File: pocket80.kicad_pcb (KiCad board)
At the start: 2 copper layers, 118 parts, among them J1 USB_C_Receptacle_USB2.0_14P, Q1 IRLML6402, Q2 BC847, SW1 F1, SW10 4, SW11 9, SW12 5, SW13 A, SW14 6, SW15 B, SW16 7, SW17 0, SW18 INC, SW19 1, SW2 F2, SW20 DEC, SW21 2, SW22 SEL, SW23 3, SW24 GO!, SW25 SW_Push_DPDT, SW3 F3, SW4 F4, SW5 C, SW6 D, SW7 E, SW8 F, SW9 8, U1 Z80CPU, U10 74HC00, U11 74HC138, U12 CH340N, U13 TP4056-42-ESOP8, U14 SX1308, U15 LM393, U2 74HC244, U3 PIO-PLCC-44, U4 SIO3-PLCC-44, U5 CTC-PLCC-44, U6 NE555D, U7 74HC04, U8 62256, U9 KM28C64A, Y1 3.6864M

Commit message: HW: Finish CTC sound generator
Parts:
- added C29: 1u, Capacitor_SMD:C_0805_2012Metric, B.Cu at (-73.7, 53.1)
- added C30: 100n, Capacitor_SMD:C_0805_2012Metric, F.Cu at (139.9, 88.2)
- added H1: MountingHole_Pad_MP, MountingHole:MountingHole_3.2mm_M3_Pad_Via, F.Cu at (40.6, 52.5)
- added H2: MountingHole_Pad_MP, MountingHole:MountingHole_3.2mm_M3_Pad_Via, F.Cu at (40.6, 60.4)
- added H3: MountingHole_Pad_MP, MountingHole:MountingHole_3.2mm_M3_Pad_Via, F.Cu at (40.6, 68.4)
- added H4: MountingHole_Pad_MP, MountingHole:MountingHole_3.2mm_M3_Pad_Via, F.Cu at (40.6, 76.3)
- added R32: 100k, Resistor_SMD:R_0805_2012Metric, B.Cu at (-73.9, 68.1)
- added U16: 74HC74, Package_SO:SO-14_3.9x8.65mm_P1.27mm, B.Cu at (-60.4, 48.2)
- LS1, Q2, R24, R25: moved to B.Cu
- moved Q2 254.7 mm to (-71.3, 50.2), turned to 180 degrees
- moved R24 249.8 mm to (-68.2, 50.2), turned to 90 degrees
- moved R25 248.5 mm to (-66.2, 50.2), turned to 90 degrees
- moved LS1 240.0 mm to (-68.6, 60.7)
- moved C19 86.0 mm to (229.6, 119.6), turned to 90 degrees
- moved C20 82.6 mm to (227.6, 119.6), turned to 90 degrees
- moved R13 76.8 mm to (222.2, 119.1), turned to 90 degrees
- moved R14 71.6 mm to (222.2, 115.6), turned to 90 degrees
- moved L1 68.5 mm to (226.8, 111.0), turned to 180 degrees
- moved R15 66.6 mm to (222.2, 112.0), turned to 90 degrees
- moved C27 66.0 mm to (233.2, 116.8), turned to 90 degrees
- moved D7 58.1 mm to (224.8, 117.6), turned to 90 degrees
- moved U14 57.5 mm to (228.6, 116.1)
- moved U10 0.25 mm to (69.8, -51.1)
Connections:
- LS1 pad 1: Net-(Q2-C) -> Net-(C29-Pad2)
- R25 pad 1: Net-(U5-ZC/TO1) -> Net-(U16B-Q)
- U5 pad 10: unconnected-(U5-ZC/TO0-Pad10) -> /CTC/TO0
- U5 pad 12: Net-(U5-ZC/TO1) -> /CTC/TO1
- U5 pad 13: /CTC/TO2 -> Net-(U16B-C)

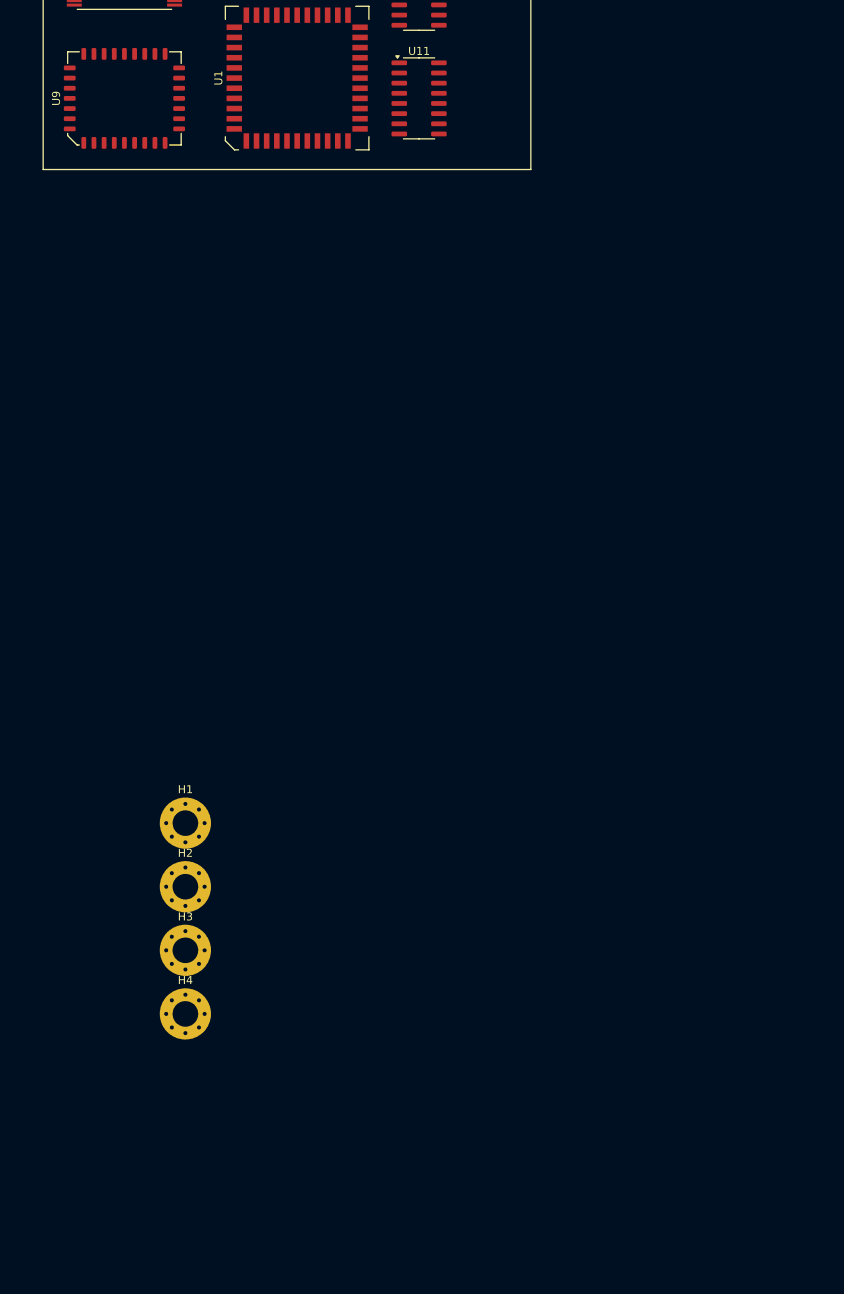
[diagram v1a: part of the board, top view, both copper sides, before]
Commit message: HW: Replace 28C64/27C64 EEPROM with 28C256
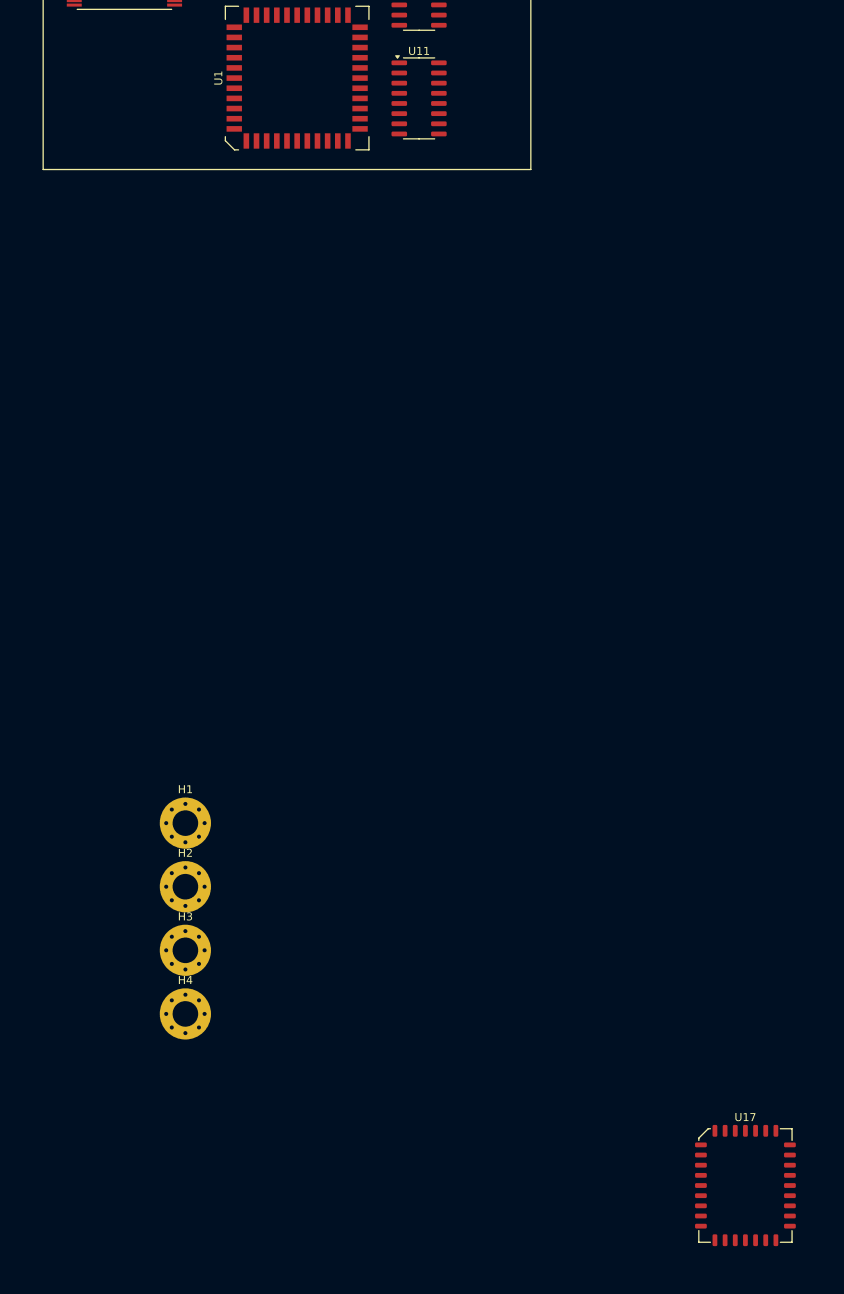
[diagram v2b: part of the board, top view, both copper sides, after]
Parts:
- removed U9: KM28C64A, Package_LCC:PLCC-32_11.4x14.0mm_P1.27mm
- added U17: 28C256, Package_LCC:PLCC-32_11.4x14.0mm_P1.27mm, F.Cu at (110.6, 97.8)

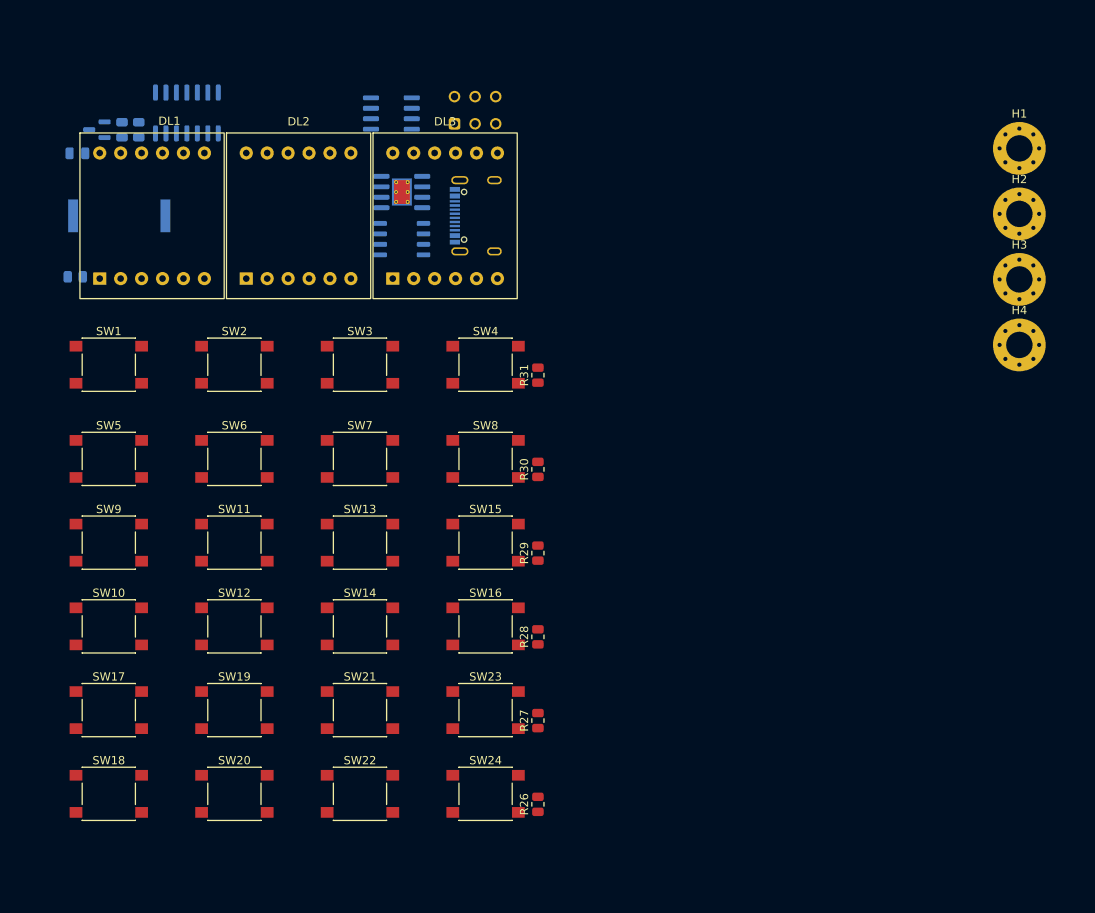
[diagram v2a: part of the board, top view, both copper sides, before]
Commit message: HW: Add rst button, sync pins
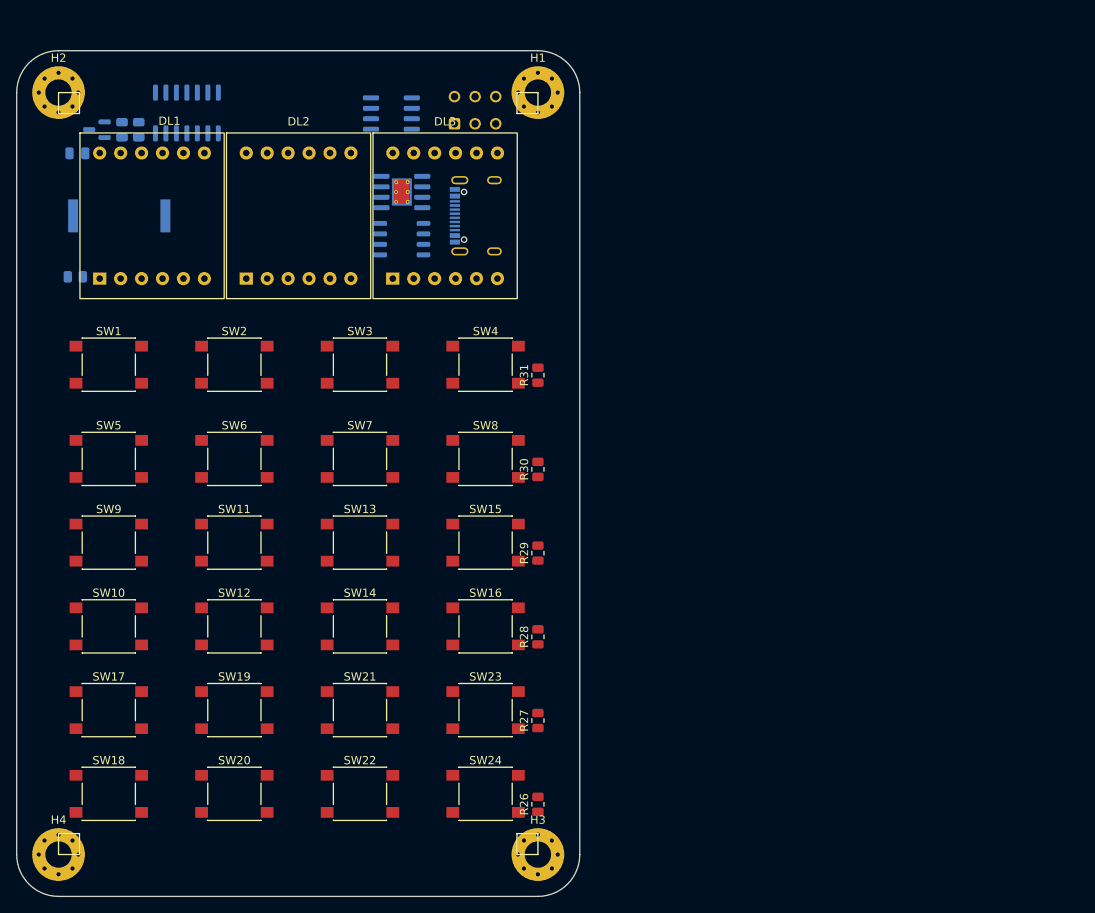
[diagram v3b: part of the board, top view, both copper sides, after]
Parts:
- moved H4 132.0 mm to (-75.9, 138.2)
- moved H2 117.5 mm to (-75.9, 45.7)
- moved H3 91.0 mm to (-17.8, 138.2)
- moved H1 58.8 mm to (-17.8, 45.7)
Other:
- board outline added: 68.3 x 102.6 mm
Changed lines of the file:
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@@
 	(footprint "MountingHole:MountingHole_3.2mm_M3_Pad_Via"
 		(layer "F.Cu")
-		(at 40.64 76.34)
+		(at -75.946 138.176)
 		(descr "Mounting Hole 3.2mm, M3")
 		(tags "mounting hole 3.2mm m3")
@@
 	(footprint "MountingHole:MountingHole_3.2mm_M3_Pad_Via"
 		(layer "F.Cu")
-		(at 40.64 60.44)
+		(at -75.946 45.72)
 		(descr "Mounting Hole 3.2mm, M3")
 		(tags "mounting hole 3.2mm m3")
@@
 	(footprint "MountingHole:MountingHole_3.2mm_M3_Pad_Via"
 		(layer "F.Cu")
-		(at 40.64 52.49)
+		(at -17.78 45.72)
 		(descr "Mounting Hole 3.2mm, M3")
 		(tags "mounting hole 3.2mm m3")
@@
 	(footprint "MountingHole:MountingHole_3.2mm_M3_Pad_Via"
 		(layer "F.Cu")
-		(at 40.64 68.39)
+		(at -17.78 138.176)
 		(descr "Mounting Hole 3.2mm, M3")
 		(tags "mounting hole 3.2mm m3")
@@
 	)
 	(gr_rect
+		(start -20.32 135.636)
+		(end -17.78 138.176)
+		(stroke
+			(width 0.1)
+			(type default)
+		)
+		(fill no)
+		(layer "F.SilkS")
+	)
+	(gr_rect
+		(start -75.946 135.636)
+		(end -73.406 138.176)
+		(stroke
+			(width 0.1)
+			(type default)
+		)
+		(fill no)
+		(layer "F.SilkS")
+	)
+	(gr_rect
+		(start -20.32 45.72)
+		(end -17.78 48.26)
+		(stroke
+			(width 0.1)
+			(type default)
+		)
+		(fill no)
+		(layer "F.SilkS")
+	)
+	(gr_rect
 		(start 22.86 -95.25)
 		(end 83.82 -29.21)
@@
 		(layer "F.SilkS")
 	)
+	(gr_rect
+		(start -75.946 45.72)
+		(end -73.406 48.26)
+		(stroke
+			(width 0.1)
+			(type default)
+		)
+		(fill no)
+		(layer "F.SilkS")
+	)
+	(gr_arc
+		(start -75.946 143.256)
+		(mid -79.538102 141.768102)
+		(end -81.026 138.176)
+		(stroke
+			(width 0.05)
+			(type default)
+		)
+		(layer "Edge.Cuts")
+	)
+	(gr_arc
+		(start -17.78 40.64)
+		(mid -14.187898 42.127898)
+		(end -12.7 45.72)
+		(stroke
+			(width 0.05)
+			(type default)
+		)
+		(layer "Edge.Cuts")
+	)
+	(gr_line
+		(start -75.945998 40.64)
+		(end -17.78 40.64)
+		(stroke
+			(width 0.05)
+			(type default)
+		)
+		(layer "Edge.Cuts")
+	)
+	(gr_line
+		(start -81.025999 138.176)
+		(end -81.025999 45.720002)
+		(stroke
+			(width 0.05)
+			(type default)
+		)
+		(layer "Edge.Cuts")
+	)
+	(gr_line
+		(start -17.780002 143.256)
+		(end -75.946 143.256)
+		(stroke
+			(width 0.05)
+			(type default)
+		)
+		(layer "Edge.Cuts")
+	)
+	(gr_arc
+		(start -81.026 45.72)
+		(mid -79.538102 42.127898)
+		(end -75.946 40.64)
+		(stroke
+			(width 0.05)
+			(type default)
+		)
+		(layer "Edge.Cuts")
+	)
+	(gr_arc
+		(start -12.7 138.176)
+		(mid -14.187898 141.768102)
+		(end -17.78 143.256)
+		(stroke
+			(width 0.05)
+			(type default)
+		)
+		(layer "Edge.Cuts")
+	)
+	(gr_line
+		(start -12.7 45.72)
+		(end -12.7 138.175998)
+		(stroke
+			(width 0.05)
+			(type default)
+		)
+		(layer "Edge.Cuts")
+	)
 	(embedded_fonts no)

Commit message: HW: Start final placement
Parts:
- added C31: 100n, Capacitor_SMD:C_0805_2012Metric, B.Cu at (-54.4, 48.8)
- added D11: 1N4148, Diode_SMD:D_MiniMELF, B.Cu at (-58.2, 40.6)
- added D12: 1N4148, Diode_SMD:D_MiniMELF, B.Cu at (-58.2, 42.9)
- added D13: HEARTBEAT, LED_SMD:LED_0805_2012Metric, F.Cu at (-35.3, 38.9)
- added J2: Conn_02x10_Odd_Even, Connector_PinSocket_2.54mm:PinSocket_2x10_P2.54mm_Horizontal, B.Cu at (-48.3, 48.8)
- added R33: 4K7, Resistor_SMD:R_0805_2012Metric, B.Cu at (-52.1, 43.9)
- added R34: 4K7, Resistor_SMD:R_0805_2012Metric, B.Cu at (-52.1, 41.9)
- added R35: 470R, Resistor_SMD:R_0805_2012Metric, F.Cu at (-31.2, 43.4)
- added SW26: RESET, Button_Switch_SMD:SW_SPST_PTS645, F.Cu at (-77.2, 50.8)
- added U9: 24C512, Package_SO:SOIC-8_3.9x4.9mm_P1.27mm, B.Cu at (-58.2, 48.0)
- C1, C14, C17, C19, C2, C20, C27, C3, C8, D7, L1, Q1, R1, R10, R12, R13, R14, R15, R16, R19, R2, R20, R21, R9, U14, U6: moved to B.Cu
- D3, D4, D5: footprint Diode_SMD:D_MicroMELF -> Diode_SMD:D_MiniMELF
- LS1, U15, U16: moved to F.Cu
- moved C27 290.9 mm to (-52.3, 61.0), turned to -90 degrees
- moved C19 284.5 mm to (-48.0, 57.4), turned to 0 degrees
- moved C20 282.1 mm to (-48.0, 59.4), turned to 0 degrees
- moved U14 279.1 mm to (-44.5, 58.4), turned to 90 degrees
- moved D7 276.4 mm to (-46.0, 62.2), turned to 0 degrees
- moved R13 275.2 mm to (-47.5, 64.8), turned to 0 degrees
- moved L1 271.0 mm to (-39.4, 60.2), turned to -90 degrees
- moved R14 271.0 mm to (-43.9, 64.8), turned to 0 degrees
- moved R15 266.9 mm to (-40.4, 64.8), turned to 0 degrees
- moved R21 235.2 mm to (-52.1, 39.9)
- moved R20 234.5 mm to (-52.1, 46.0), turned to 180 degrees
- moved R19 233.5 mm to (-51.3, 48.8), turned to 90 degrees
- moved R1 230.3 mm to (-76.5, 56.9)
- moved R2 230.2 mm to (-73.2, 46.5), turned to -90 degrees
- moved D6 227.3 mm to (-40.1, 39.9), turned to 180 degrees
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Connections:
- net Net-(D6-A) renamed VBUS
- D2 pad 1: /Keyboard/A0 -> /CPU/A0
- D3 pad 1: /Keyboard/A1 -> /CPU/A1
- D4 pad 1: /Keyboard/A2 -> /CPU/A2
- D5 pad 1: /Keyboard/A3 -> /CPU/A3
- D8 pad 2: +BATT -> VCC
- DL1 pad 1: /Display/D5 -> /CPU/D5
- DL1 pad 10: /Display/D2 -> /CPU/D2
- DL1 pad 11: /Display/D3 -> /CPU/D3
- DL1 pad 12: /Display/D6 -> /CPU/D6
- DL1 pad 2: /Display/D4 -> /CPU/D4
- DL1 pad 3: /Display/~{DISP_1} -> /CPU/~{DISP1}
- DL1 pad 4: /Display/A1 -> /CPU/A1
- DL1 pad 5: /Display/A0 -> /CPU/A0
- DL1 pad 8: /Display/D0 -> /CPU/D0
- DL1 pad 9: /Display/D1 -> /CPU/D1
- DL2 pad 1: /Display/D5 -> /CPU/D5
- DL2 pad 10: /Display/D2 -> /CPU/D2
- DL2 pad 11: /Display/D3 -> /CPU/D3
- DL2 pad 12: /Display/D6 -> /CPU/D6
- DL2 pad 2: /Display/D4 -> /CPU/D4
- DL2 pad 3: /Display/~{DISP_2} -> /CPU/~{DISP2}
- DL2 pad 4: /Display/A1 -> /CPU/A1
- DL2 pad 5: /Display/A0 -> /CPU/A0
- DL2 pad 8: /Display/D0 -> /CPU/D0
- DL2 pad 9: /Display/D1 -> /CPU/D1
- DL3 pad 1: /Display/D5 -> /CPU/D5
- DL3 pad 10: /Display/D2 -> /CPU/D2
- DL3 pad 11: /Display/D3 -> /CPU/D3
- DL3 pad 12: /Display/D6 -> /CPU/D6
- DL3 pad 2: /Display/D4 -> /CPU/D4
- DL3 pad 3: /Display/~{DISP_3} -> /CPU/~{DISP3}
- DL3 pad 4: /Display/A1 -> /CPU/A1
- DL3 pad 5: /Display/A0 -> /CPU/A0
- DL3 pad 8: /Display/D0 -> /CPU/D0
- DL3 pad 9: /Display/D1 -> /CPU/D1
- R10 pad 2: /USB and power/RX -> /SIO/TX1
- R17 pad 2: Net-(R17-Pad2) -> GND
- R9 pad 1: /USB and power/TX -> /SIO/RX1
- SW25 pad 5: Net-(R17-Pad2) -> Net-(Q1-G)
- U11 pad 10: /CPU/~{DISP_0} -> /CPU/~{DISP1}
- U11 pad 12: unconnected-(U11-~{Y3}-Pad12) -> /CPU/~{SRST}
- U11 pad 7: /CPU/~{DISP_2} -> /CPU/~{DISP3}
- U11 pad 9: /CPU/~{DISP_1} -> /CPU/~{DISP2}
- U16 pad 13: /CTC/~{SRST} -> /CPU/~{SRST}
- U17 pad 10: /Memory/A1 -> /CPU/A1
- U17 pad 11: /Memory/A0 -> /CPU/A0
- U17 pad 13: /Memory/D0 -> /CPU/D0
- U17 pad 14: /Memory/D1 -> /CPU/D1
- U17 pad 15: /Memory/D2 -> /CPU/D2
- U17 pad 18: /Memory/D3 -> /CPU/D3
- U17 pad 19: /Memory/D4 -> /CPU/D4
- U17 pad 2: /Memory/A14 -> /CPU/A14
- U17 pad 20: /Memory/D5 -> /CPU/D5
- U17 pad 21: /Memory/D6 -> /CPU/D6
- U17 pad 22: /Memory/D7 -> /CPU/D7
- U17 pad 23: /Memory/~{ROM} -> /CPU/~{ROM}
- U17 pad 24: /Memory/A10 -> /CPU/A10
- U17 pad 25: /Memory/~{RD} -> /CPU/~{RD}
- U17 pad 27: /Memory/A11 -> /CPU/A11
- U17 pad 28: /Memory/A9 -> /CPU/A9
- U17 pad 29: /Memory/A8 -> /CPU/A8
- U17 pad 3: /Memory/A12 -> /CPU/A12
- U17 pad 30: /Memory/A13 -> /CPU/A13
- U17 pad 31: /Memory/~{WR} -> /CPU/~{WR}
- U17 pad 4: /Memory/A7 -> /CPU/A7
- U17 pad 5: /Memory/A6 -> /CPU/A6
- U17 pad 6: /Memory/A5 -> /CPU/A5
- U17 pad 7: /Memory/A4 -> /CPU/A4
- U17 pad 8: /Memory/A3 -> /CPU/A3
- U17 pad 9: /Memory/A2 -> /CPU/A2
- U2 pad 1: /Keyboard/~{KEYBOARD} -> /CPU/~{KEY}
- U2 pad 12: /Keyboard/D3 -> /CPU/D3
- U2 pad 14: /Keyboard/D2 -> /CPU/D2
- U2 pad 16: /Keyboard/D1 -> /CPU/D1
- U2 pad 18: /Keyboard/D0 -> /CPU/D0
- U2 pad 19: /Keyboard/~{KEYBOARD} -> /CPU/~{KEY}
- U2 pad 3: /Keyboard/D4 -> /CPU/D4
- U2 pad 5: /Keyboard/D5 -> /CPU/D5
- U3 pad 1: /PIO/D2 -> /CPU/D2
- U3 pad 10: unconnected-(U3-PA5-Pad10) -> /Expansion/PORTA5
- U3 pad 11: unconnected-(U3-PA4-Pad11) -> /Expansion/PORTA4
- U3 pad 14: unconnected-(U3-PA3-Pad14) -> /Expansion/PORTA3
- U3 pad 15: unconnected-(U3-PA2-Pad15) -> /Expansion/PORTA2
- U3 pad 16: unconnected-(U3-PA1-Pad16) -> /Expansion/PORTA1
- U3 pad 17: unconnected-(U3-PA0-Pad17) -> /Expansion/PORTA0
- U3 pad 18: unconnected-(U3-~{ASTB}-Pad18) -> /Expansion/~{ASTB}
- U3 pad 19: unconnected-(U3-~{BSTB}-Pad19) -> VCC
- U3 pad 2: /PIO/D7 -> /CPU/D7
- U3 pad 20: unconnected-(U3-ARDY-Pad20) -> /Expansion/ARDY
- U3 pad 21: /PIO/D0 -> /CPU/D0
- U3 pad 22: /PIO/D1 -> /CPU/D1
- U3 pad 27: /PIO/~{INT} -> /CPU/~{INT}
- U3 pad 29: /PIO/CLK -> /CPU/CLK
- U3 pad 3: /PIO/D6 -> /CPU/D6
- U3 pad 31: unconnected-(U3-PB0-Pad31) -> /Expansion/PORTB0
- U3 pad 32: unconnected-(U3-PB1-Pad32) -> /Expansion/PORTB1
- U3 pad 33: unconnected-(U3-PB2-Pad33) -> Net-(U3-PB2)
- U3 pad 35: unconnected-(U3-PB4-Pad35) -> Net-(D12-K)
- U3 pad 36: unconnected-(U3-PB5-Pad36) -> Net-(D11-K)
- U3 pad 37: unconnected-(U3-PB6-Pad37) -> Net-(D12-A)
- U3 pad 38: unconnected-(U3-PB7-Pad38) -> Net-(D11-A)
- U3 pad 39: /PIO/~{RD} -> /CPU/~{RD}
- U3 pad 4: /PIO/~{PIO} -> /CPU/~{PIO}
- U3 pad 40: /PIO/~{IOREQ} -> /CPU/~{IOREQ}
- U3 pad 41: /PIO/~{M1} -> /CPU/~{PIO_M1}
- U3 pad 42: /PIO/D5 -> /CPU/D5
- U3 pad 43: /PIO/D4 -> /CPU/D4
- U3 pad 44: /PIO/D3 -> /CPU/D3
- U3 pad 5: /PIO/A1 -> /CPU/A1
- U3 pad 7: /PIO/A0 -> /CPU/A0
- U3 pad 8: unconnected-(U3-PA7-Pad8) -> /Expansion/PORTA7
- U3 pad 9: unconnected-(U3-PA6-Pad9) -> /Expansion/PORTA6
- U4 pad 1: /SIO/D0 -> /CPU/D0
- U4 pad 14: /SIO/BAUD1 -> /CTC/TO1
- U4 pad 15: /SIO/BAUD1 -> /CTC/TO1
- U4 pad 2: /SIO/D1 -> /CPU/D1
- U4 pad 22: /SIO/CLK -> /CPU/CLK
- U4 pad 23: /SIO/~{RST} -> /CPU/~{RST}
- U4 pad 3: /SIO/D3 -> /CPU/D3
- U4 pad 30: /SIO/TX2 -> /Expansion/RX
- U4 pad 31: /SIO/BAUD2 -> /CTC/TO1
- U4 pad 32: /SIO/BAUD2 -> /CTC/TO1
- U4 pad 33: /SIO/RX2 -> /Expansion/TX
- U4 pad 37: /SIO/~{RD} -> /CPU/~{RD}
- U4 pad 38: /SIO/A1 -> /CPU/A1
- U4 pad 39: /SIO/A0 -> /CPU/A0
- U4 pad 4: /SIO/D5 -> /CPU/D5
- U4 pad 40: /SIO/~{SIO} -> /CPU/~{SIO}
- U4 pad 41: /SIO/~{IOREQ} -> /CPU/~{IOREQ}
- U4 pad 42: /SIO/D6 -> /CPU/D6
- U4 pad 43: /SIO/D4 -> /CPU/D4
- U4 pad 44: /SIO/D2 -> /CPU/D2
- U4 pad 5: /SIO/D7 -> /CPU/D7
- U4 pad 6: /SIO/~{INT} -> /CPU/~{INT}
- U4 pad 7: /SIO/IEI -> /CTC/IEO
- U4 pad 8: /SIO/IEO -> /PIO/IEI
- U4 pad 9: /SIO/~{M1} -> /CPU/~{M1}
- U5 pad 1: /CTC/D4 -> /CPU/D4
- U5 pad 14: /CTC/~{IOREQ} -> /CPU/~{IOREQ}
- U5 pad 19: /CTC/~{INT} -> /CPU/~{INT}
- U5 pad 2: /CTC/D5 -> /CPU/D5
- U5 pad 22: /CTC/~{M1} -> /CPU/~{M1}
- U5 pad 24: /CTC/CLK -> /CPU/CLK
- U5 pad 25: /CTC/~{CTC} -> /CPU/~{CTC}
- U5 pad 26: /CTC/~{RST} -> /CPU/~{RST}
- U5 pad 27: /CTC/A0 -> /CPU/A0
- U5 pad 29: /CTC/A1 -> /CPU/A1
- U5 pad 4: /CTC/D6 -> /CPU/D6
- U5 pad 41: /CTC/D0 -> /CPU/D0
- U5 pad 42: /CTC/D1 -> /CPU/D1
- U5 pad 43: /CTC/D2 -> /CPU/D2
- U5 pad 44: /CTC/D3 -> /CPU/D3
- U5 pad 5: /CTC/D7 -> /CPU/D7
- U5 pad 9: /CTC/~{RD} -> /CPU/~{RD}
- U8 pad 1: /Memory/~{RD} -> /CPU/~{RD}
- U8 pad 10: /Memory/A7 -> /CPU/A7
- U8 pad 11: /Memory/A6 -> /CPU/A6
- U8 pad 12: /Memory/A5 -> /CPU/A5
- U8 pad 13: /Memory/A4 -> /CPU/A4
- U8 pad 14: /Memory/A3 -> /CPU/A3
- U8 pad 15: /Memory/A2 -> /CPU/A2
- U8 pad 16: /Memory/A1 -> /CPU/A1
- U8 pad 17: /Memory/A0 -> /CPU/A0
- U8 pad 18: /Memory/D0 -> /CPU/D0
- U8 pad 19: /Memory/D1 -> /CPU/D1
- U8 pad 2: /Memory/A11 -> /CPU/A11
- U8 pad 20: /Memory/D2 -> /CPU/D2
- U8 pad 22: /Memory/D3 -> /CPU/D3
- U8 pad 23: /Memory/D4 -> /CPU/D4
- U8 pad 24: /Memory/D5 -> /CPU/D5
- U8 pad 25: /Memory/D6 -> /CPU/D6
- U8 pad 26: /Memory/D7 -> /CPU/D7
- U8 pad 27: /Memory/~{RAM} -> /CPU/~{RAM}
- U8 pad 28: /Memory/A10 -> /CPU/A10
- U8 pad 3: /Memory/A9 -> /CPU/A9
- U8 pad 4: /Memory/A8 -> /CPU/A8
- U8 pad 5: /Memory/A13 -> /CPU/A13
- U8 pad 6: /Memory/~{WR} -> /CPU/~{WR}
- U8 pad 8: /Memory/A14 -> /CPU/A14
- U8 pad 9: /Memory/A12 -> /CPU/A12
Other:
- board size 68.3 x 102.6 mm -> 68.6 x 107.3 mm

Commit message: HW: Fix mounting holes
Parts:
- C10, C4, C5, C9, R3, R4, U1, U10, U11, U17, U2, U3, U4, U5, U7, U8: moved to B.Cu
- moved R4 225.8 mm to (-70.1, 58.2), turned to -90 degrees
- moved R3 224.3 mm to (-70.1, 61.7), turned to 90 degrees
- moved C5 219.5 mm to (-70.9, 55.4), turned to 180 degrees
- moved C4 216.5 mm to (-70.9, 64.5), turned to 180 degrees
- moved C10 210.9 mm to (-60.2, 56.4), turned to -90 degrees
- moved C9 209.3 mm to (-61.2, 66.0), turned to 180 degrees
- moved Y1 203.6 mm to (-77.2, 63.2)
- moved U8 190.9 mm to (73.0, 133.3), turned to 180 degrees
- moved U4 190.2 mm to (75.5, 115.6), turned to 0 degrees
- moved U1 190.1 mm to (73.0, 148.6), turned to -90 degrees
- moved U5 188.0 mm to (50.1, 125.7), turned to -90 degrees
- moved U2 187.8 mm to (75.5, 95.2), turned to -90 degrees
- moved U3 184.2 mm to (50.1, 100.3), turned to -90 degrees
- moved U7 183.2 mm to (-65.3, 60.2), turned to 180 degrees
- moved U11 172.6 mm to (89.5, 133.3), turned to 180 degrees
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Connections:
- H1 pad 1: (no net) -> GND
- H2 pad 1: (no net) -> GND
- H3 pad 1: (no net) -> GND
- H4 pad 1: (no net) -> GND
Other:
- copper layers 2 -> 4

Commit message: HW: placement finished
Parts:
- C15, C16, C18, C26, C28, C30, R18, Y1: moved to B.Cu
- D2: footprint Diode_SMD:D_MicroMELF -> Diode_SMD:D_MiniMELF
- moved Y1 179.6 mm to (102.4, 64.3)
- moved D11 178.3 mm to (120.1, 40.4), turned to -90 degrees
- moved R33 177.8 mm to (125.7, 40.9), turned to 0 degrees
- moved U15 177.8 mm to (132.1, 39.6)
- moved U13 177.8 mm to (152.7, 56.9)
- moved C1 177.8 mm to (104.9, 56.4)
- moved C10 177.8 mm to (117.6, 55.4)
- moved C14 177.8 mm to (147.1, 60.5)
- moved C17 177.8 mm to (143.0, 57.7)
- moved C19 177.8 mm to (129.8, 56.4)
- moved C2 177.8 mm to (100.6, 46.0)
- moved C20 177.8 mm to (129.8, 58.4)
- moved C27 177.8 mm to (123.4, 55.9)
- moved C29 177.8 mm to (114.8, 46.0)
- moved C3 177.8 mm to (102.6, 46.0)
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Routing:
- net /CPU/D0: track 0.00 -> 96.4 mm, vias 0 -> 2
- net /CPU/D2: track 0.00 -> 89.0 mm, vias 0 -> 5
- net /CPU/D1: track 0.00 -> 77.8 mm, vias 0 -> 3
- net /CPU/D3: track 0.00 -> 76.7 mm, vias 0 -> 5
- net /CPU/A0: track 0.00 -> 73.6 mm, vias 0 -> 2
- net /CPU/D4: track 0.00 -> 73.3 mm, vias 0 -> 5
- net /CPU/A1: track 0.00 -> 69.4 mm, vias 0 -> 2
- net /CPU/A3: track 0.00 -> 67.8 mm, vias 0 -> 2
- net /CPU/A4: track 0.00 -> 66.0 mm, vias 0 -> 2
- net /CPU/A2: track 0.00 -> 65.1 mm, vias 0 -> 2
- net /CPU/D5: track 0.00 -> 64.9 mm, vias 0 -> 5
- net /CPU/A5: track 0.00 -> 63.1 mm, vias 0 -> 2
- net /CPU/A6: track 0.00 -> 60.3 mm, vias 0 -> 2
- net /CPU/A14: track 0.00 -> 57.0 mm, vias 0 -> 4
- net /CPU/A12: track 0.00 -> 55.4 mm, vias 0 -> 4
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- added copper zone on B.Cu, net Net-(D7-A)
- added copper zone on B.Cu, net Net-(Q1-D)
- added copper zone on B.Cu, net VCC
